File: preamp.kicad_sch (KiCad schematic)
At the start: 23 parts, among them U2 TL972QDRQ1

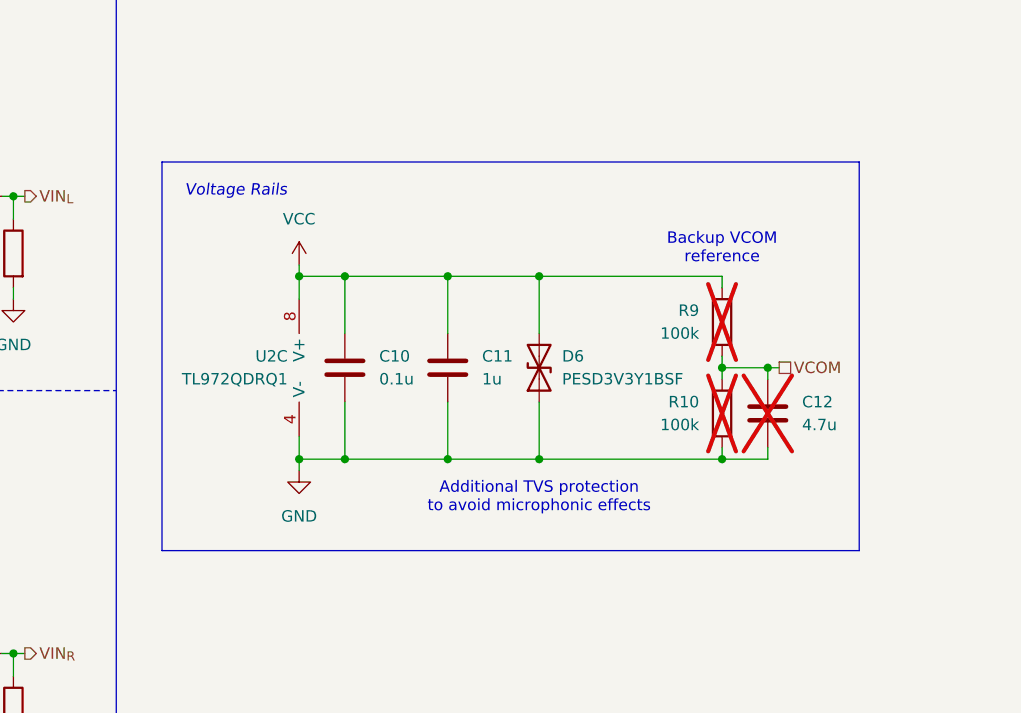
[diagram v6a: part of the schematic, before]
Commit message: Replace 0201 diodes with recommended arrays and nothing (some were spurious and I think I don't need them)
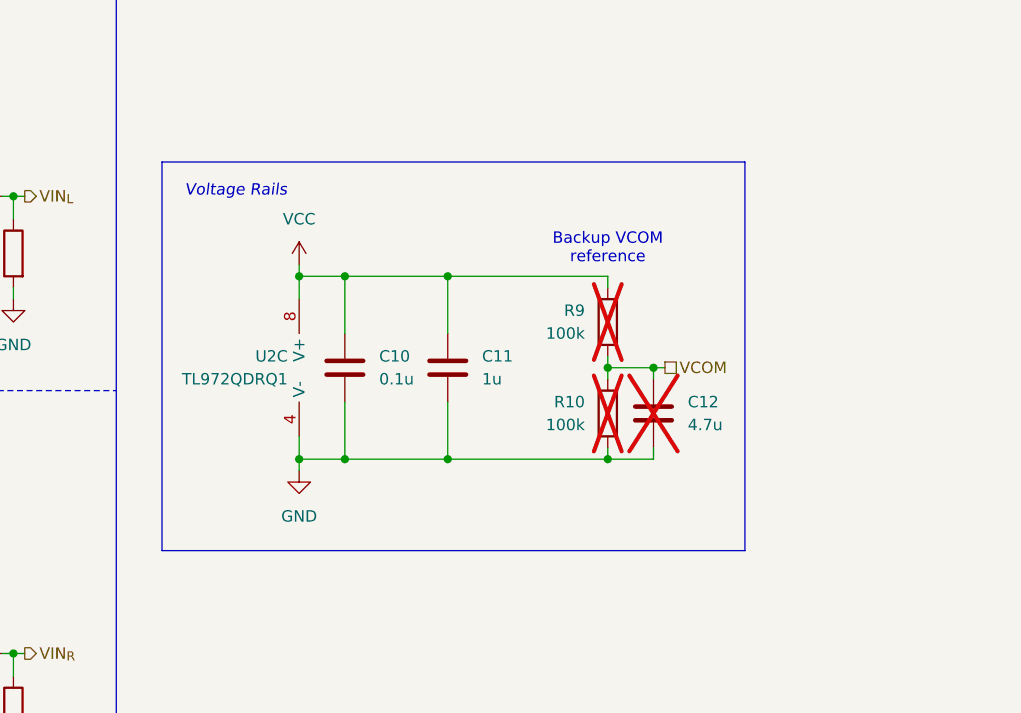
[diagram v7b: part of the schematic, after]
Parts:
- removed D6: PESD3V3Y1BSF, Diode_SMD:D_0201_0603Metric_Pad0.64x0.40mm_HandSolder, symbol Device:D_TVS
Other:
- note removed: "Additional TVS protection to avoid microphonic effects"
- moved on the sheet: C12, R10, R9
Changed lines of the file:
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@@
 	)
 	(junction
-		(at 224.79 106.68)
+		(at 212.09 106.68)
 		(diameter 0)
 		(color 0 0 0 0)
@@
 	)
 	(junction
-		(at 204.47 86.36)
-		(diameter 0)
-		(color 0 0 0 0)
-	)
-	(junction
-		(at 224.79 96.52)
+		(at 212.09 96.52)
 		(diameter 0)
 		(color 0 0 0 0)
@@
 	)
 	(junction
-		(at 204.47 106.68)
-		(diameter 0)
-		(color 0 0 0 0)
-	)
-	(junction
 		(at 99.06 67.31)
 		(diameter 0)
@@
 	)
 	(junction
-		(at 229.87 96.52)
+		(at 217.17 96.52)
 		(diameter 0)
 		(color 0 0 0 0)
@@
 	(wire
 		(pts
-			(xy 229.87 96.52) (xy 231.14 96.52)
+			(xy 217.17 96.52) (xy 218.44 96.52)
 		)
 		(stroke
@@
 	(wire
 		(pts
-			(xy 224.79 86.36) (xy 224.79 87.63)
+			(xy 212.09 86.36) (xy 212.09 87.63)
 		)
 		(stroke
@@
 	(wire
 		(pts
-			(xy 229.87 106.68) (xy 224.79 106.68)
+			(xy 217.17 106.68) (xy 212.09 106.68)
 		)
 		(stroke
@@
 	(wire
 		(pts
-			(xy 224.79 95.25) (xy 224.79 96.52)
+			(xy 212.09 95.25) (xy 212.09 96.52)
 		)
 		(stroke
@@
 	(wire
 		(pts
-			(xy 224.79 96.52) (xy 224.79 97.79)
+			(xy 212.09 96.52) (xy 212.09 97.79)
 		)
 		(stroke
@@
 	(wire
 		(pts
-			(xy 229.87 96.52) (xy 229.87 97.79)
+			(xy 217.17 96.52) (xy 217.17 97.79)
 		)
 		(stroke
@@
 	(wire
 		(pts
-			(xy 224.79 105.41) (xy 224.79 106.68)
+			(xy 212.09 105.41) (xy 212.09 106.68)
 		)
 		(stroke
@@
 	(wire
 		(pts
-			(xy 204.47 100.33) (xy 204.47 106.68)
-		)
-		(stroke
-			(width 0)
-			(type default)
-		)
-	)
-	(wire
-		(pts
 			(xy 194.31 106.68) (xy 182.88 106.68)
 		)
@@
 	(wire
 		(pts
-			(xy 204.47 106.68) (xy 224.79 106.68)
-		)
-		(stroke
-			(width 0)
-			(type default)
-		)
-	)
-	(wire
-		(pts
-			(xy 204.47 86.36) (xy 204.47 92.71)
-		)
-		(stroke
-			(width 0)
-			(type default)
-		)
-	)
-	(wire
-		(pts
 			(xy 146.05 87.63) (xy 146.05 88.9)
 		)
@@
 	(wire
 		(pts
-			(xy 204.47 86.36) (xy 224.79 86.36)
-		)
-		(stroke
-			(width 0)
-			(type default)
-		)
-	)
-	(wire
-		(pts
 			(xy 146.05 138.43) (xy 146.05 139.7)
 		)
@@
 	(wire
 		(pts
-			(xy 194.31 86.36) (xy 204.47 86.36)
+			(xy 194.31 86.36) (xy 212.09 86.36)
 		)
 		(stroke
@@
 	(wire
 		(pts
-			(xy 224.79 96.52) (xy 229.87 96.52)
+			(xy 212.09 96.52) (xy 217.17 96.52)
 		)
 		(stroke
@@
 	(wire
 		(pts
-			(xy 204.47 106.68) (xy 194.31 106.68)
+			(xy 194.31 106.68) (xy 212.09 106.68)
 		)
 		(stroke
@@
 	(wire
 		(pts
-			(xy 229.87 105.41) (xy 229.87 106.68)
+			(xy 217.17 105.41) (xy 217.17 106.68)
 		)
 		(stroke
@@
 	(rectangle
 		(start 162.56 73.66)
-		(end 240.03 116.84)
+		(end 227.33 116.84)
 		(stroke
 			(width 0)
@@
 	(text "Backup VCOM\nreference"
 		(exclude_from_sim no)
-		(at 224.79 85.09 0)
+		(at 212.09 85.09 0)
 		(effects
 			(font
@@
 		)
 	)
-	(text "Additional TVS protection\nto avoid microphonic effects"
-		(exclude_from_sim no)
-		(at 204.47 109.22 0)
-		(effects
-			(font
-				(size 1.27 1.27)
-			)
-			(justify top)
-		)
-	)
 	(text "Preamp"
 		(exclude_from_sim no)
@@
 	(hierarchical_label "VCOM"
 		(shape passive)
-		(at 231.14 96.52 0)
+		(at 218.44 96.52 0)
 		(fields_autoplaced yes)
 		(effects
@@
 	)
 	(symbol
-		(lib_id "Device:D_TVS")
-		(at 204.47 96.52 90)
-		(unit 1)
-		(exclude_from_sim no)
-		(in_bom yes)
-		(on_board yes)
-		(dnp no)
-		(fields_autoplaced yes)
-		(property "Reference" "D6"
-			(at 207.01 95.2499 90)
-			(effects
-				(font
-					(size 1.27 1.27)
-				)
-				(justify right)
-			)
-		)
-		(property "Value" "PESD3V3Y1BSF"
-			(at 207.01 97.7899 90)
-			(effects
-				(font
-					(size 1.27 1.27)
-				)
-				(justify right)
-			)
-		)
-		(property "Footprint" "Diode_SMD:D_0201_0603Metric_Pad0.64x0.40mm_HandSolder"
-			(at 204.47 96.52 0)
-			(effects
-				(font
-					(size 1.27 1.27)
-				)
-				(hide yes)
-			)
-		)
-		(property "Datasheet" "https://www.mouser.com/datasheet/2/916/PESD3V3Y1BSF-1370637.pdf"
-			(at 204.47 96.52 0)
-			(effects
-				(font
-					(size 1.27 1.27)
-				)
-				(hide yes)
-			)
-		)
-		(property "Description" "Bidirectional transient-voltage-suppression diode"
-			(at 204.47 96.52 0)
-			(effects
-				(font
-					(size 1.27 1.27)
-				)
-				(hide yes)
-			)
-		)
-		(property "Mouser Part Number" "771-PESD3V3Y1BSFYL"
-			(at 204.47 96.52 0)
-			(effects
-				(font
-					(size 1.27 1.27)
-				)
-				(hide yes)
-			)
-		)
-		(pin "2"
-		)
-		(pin "1"
-		)
-		(instances
-			(project "BinauralMic"
-				(path "/d9e790b9-8aa4-4e58-8bd7-6ef4bc890627/c3b3219f-f658-485a-9922-47cf99d00243"
-					(reference "D6")
-					(unit 1)
-				)
-			)
-		)
-	)
-	(symbol
 		(lib_id "Device:C")
-		(at 229.87 101.6 180)
+		(at 217.17 101.6 180)
 		(unit 1)
 		(exclude_from_sim no)
@@
 		(fields_autoplaced yes)
 		(property "Reference" "C12"
-			(at 233.68 100.3299 0)
+			(at 220.98 100.3299 0)
 			(effects
 				(font
@@
 		)
 		(property "Value" "4.7u"
-			(at 233.68 102.8699 0)
+			(at 220.98 102.8699 0)
 			(effects
 				(font
@@
 		)
 		(property "Footprint" "Capacitor_SMD:C_1206_3216Metric_Pad1.33x1.80mm_HandSolder"
-			(at 228.9048 97.79 0)
+			(at 216.2048 97.79 0)
 			(effects
 				(font
@@
 		)
 		(property "Datasheet" "https://www.mouser.com/datasheet/2/40/TAJ-3165264.pdf"
-			(at 229.87 101.6 0)
+			(at 217.17 101.6 0)
 			(effects
 				(font
@@
 		)
 		(property "Description" "Unpolarized capacitor"
-			(at 229.87 101.6 0)
+			(at 217.17 101.6 0)
 			(effects
 				(font
@@
 		)
 		(property "Mouser Part Number" "581-TAJA475K016R"
-			(at 229.87 101.6 0)
+			(at 217.17 101.6 0)
 			(effects
 				(font
@@
 	(symbol
 		(lib_id "Device:R")
-		(at 224.79 91.44 0)
+		(at 212.09 91.44 0)
 		(mirror y)
 		(unit 1)
@@
 		(dnp yes)
 		(property "Reference" "R9"
-			(at 222.25 90.1699 0)
+			(at 209.55 90.1699 0)
 			(effects
 				(font
@@
 		)
 		(property "Value" "100k"
-			(at 222.25 92.7099 0)
+			(at 209.55 92.7099 0)
 			(effects
 				(font
@@
 		)
 		(property "Footprint" "Resistor_SMD:R_0603_1608Metric_Pad0.98x0.95mm_HandSolder"
-			(at 226.568 91.44 90)
+			(at 213.868 91.44 90)
 			(effects
 				(font
@@
 		)
 		(property "Datasheet" "https://www.mouser.com/datasheet/2/447/PYu_RT_1_to_0_01_RoHS_L_15-3461507.pdf"
-			(at 224.79 91.44 0)
+			(at 212.09 91.44 0)
 			(effects
 				(font
@@
 		)
 		(property "Description" "Resistor"
-			(at 224.79 91.44 0)
+			(at 212.09 91.44 0)
 			(effects
 				(font
@@
 		)
 		(property "Mouser Part Number" "603-RT0603FRE10100KL"
-			(at 224.79 91.44 0)
+			(at 212.09 91.44 0)
 			(effects
 				(font
@@
 	(symbol
 		(lib_id "Device:R")
-		(at 224.79 101.6 0)
+		(at 212.09 101.6 0)
 		(mirror y)
 		(unit 1)
@@
 		(dnp yes)
 		(property "Reference" "R10"
-			(at 222.25 100.3299 0)
+			(at 209.55 100.3299 0)
 			(effects
 				(font
@@
 		)
 		(property "Value" "100k"
-			(at 222.25 102.8699 0)
+			(at 209.55 102.8699 0)
 			(effects
 				(font
@@
 		)
 		(property "Footprint" "Resistor_SMD:R_0603_1608Metric_Pad0.98x0.95mm_HandSolder"
-			(at 226.568 101.6 90)
+			(at 213.868 101.6 90)
 			(effects
 				(font
@@
 		)
 		(property "Datasheet" "https://www.mouser.com/datasheet/2/447/PYu_RT_1_to_0_01_RoHS_L_15-3461507.pdf"
-			(at 224.79 101.6 0)
+			(at 212.09 101.6 0)
 			(effects
 				(font
@@
 		)
 		(property "Description" "Resistor"
-			(at 224.79 101.6 0)
+			(at 212.09 101.6 0)
 			(effects
 				(font
@@
 		)
 		(property "Mouser Part Number" "603-RT0603FRE10100KL"
-			(at 224.79 101.6 0)
+			(at 212.09 101.6 0)
 			(effects
 				(font
